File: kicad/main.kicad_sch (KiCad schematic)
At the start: 21 parts, among them J1 ICSP header, J2 LOAD+, J3 LOAD-, J4 BAT+, J5 BAT-, SW1 SW_SPST, U1 ATtiny13-20SS, U2 AO3406

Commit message: light duration settings
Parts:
- SW1: footprint Button_Switch_SMD:SW_Push_SPST_NO_Alps_SKRK -> Button_Switch_THT:SW_PUSH_6mm
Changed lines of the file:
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@@
     (property "Reference" "SW1" (id 0) (at 167.64 133.985 0))
     (property "Value" "SW_SPST" (id 1) (at 167.64 136.7601 0))
-    (property "Footprint" "Button_Switch_SMD:SW_Push_SPST_NO_Alps_SKRK" (id 2) (at 170.18 131.445 0)
+    (property "Footprint" "Button_Switch_THT:SW_PUSH_6mm" (id 2) (at 170.18 131.445 0)
       (effects (font (size 1.27 1.27)) hide)
     )
@@
     )
     (path "/02eed7f8-646e-4c7f-abe4-21cd29a1e93f"
-      (reference "SW1") (unit 1) (value "SW_SPST") (footprint "Button_Switch_SMD:SW_Push_SPST_NO_Alps_SKRK")
+      (reference "SW1") (unit 1) (value "SW_SPST") (footprint "Button_Switch_THT:SW_PUSH_6mm")
     )
     (path "/a5624d14-534e-4568-b415-af0009b2ac24"

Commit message: clean up
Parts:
- removed D1: RED, LED_SMD:LED_0805_2012Metric, symbol Device:LED
- removed H2: MountingHole, MountingHole:MountingHole_2.2mm_M2, symbol Mechanical:MountingHole
- removed J2: LOAD+, Connector_Pin:Pin_D1.0mm_L10.0mm, symbol Connector:Conn_01x01_Female
- removed J3: LOAD-, Connector_Pin:Pin_D1.0mm_L10.0mm, symbol Connector:Conn_01x01_Female
- removed R2: LDR, Connector_PinSocket_2.54mm:PinSocket_2x01_P2.54mm_Vertical, symbol Device:R_US
- removed R3: 10k, Resistor_SMD:R_0805_2012Metric, symbol Device:R_US
- added J2: Conn_LOAD, Connector_JST:JST_XH_B2B-XH-A_1x02_P2.50mm_Vertical, symbol Connector:Conn_01x02_Female
- added R2: LDR07, OptoDevice:R_LDR_5.1x4.3mm_P3.4mm_Vertical, symbol Sensor_Optical:LDR07
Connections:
- net MOSI is gone; now on net GATE: J1.4 (Pin_4), U1.5 (PB0)
- net GND: now also R2.2
- net VCC: now also J2.1 (Pin_1); no longer R1.2
- net V_REF: now also U1.3 (PB4), R2.1; no longer U1.2 (PB3)
- net at D2.1 (K), U2.3 (D): now also J2.2 (Pin_2)
- net GATE: now reaches R5.2
- net GATE: no longer U1.3 (PB4)
- new net ADC_PWR: R1.2, U1.2 (PB3)
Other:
- note added: "internal pull-up"
- moved on the sheet: D2, J1, R1, R5, R6, R7, SW1, U2

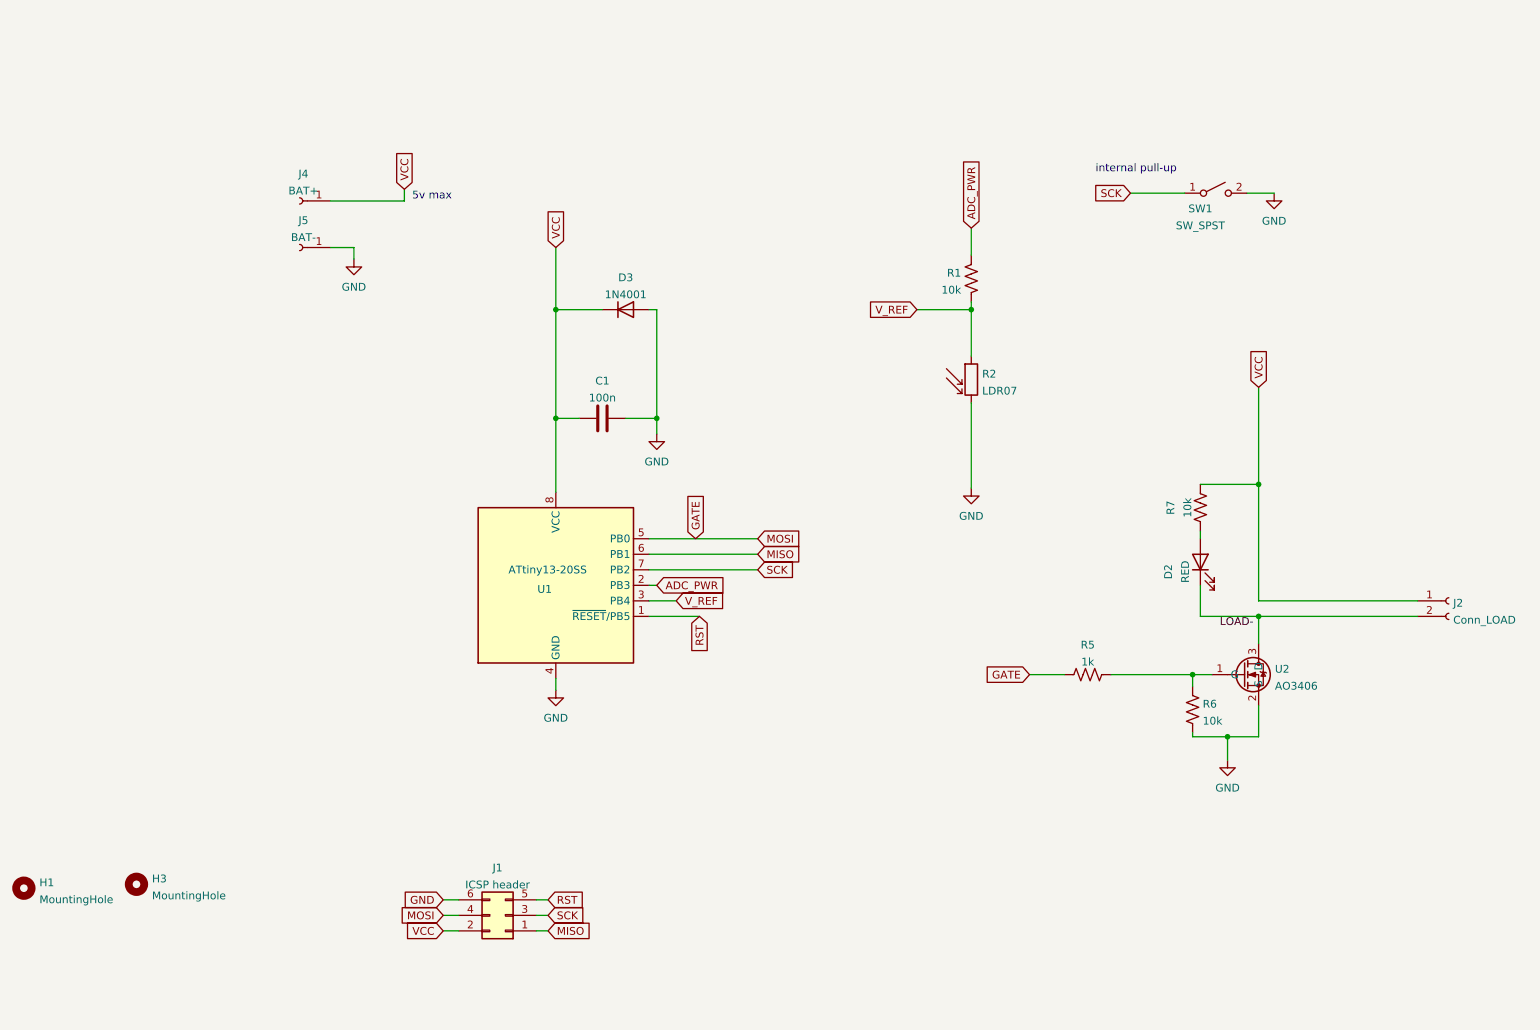
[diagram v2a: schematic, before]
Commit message: add README description and images
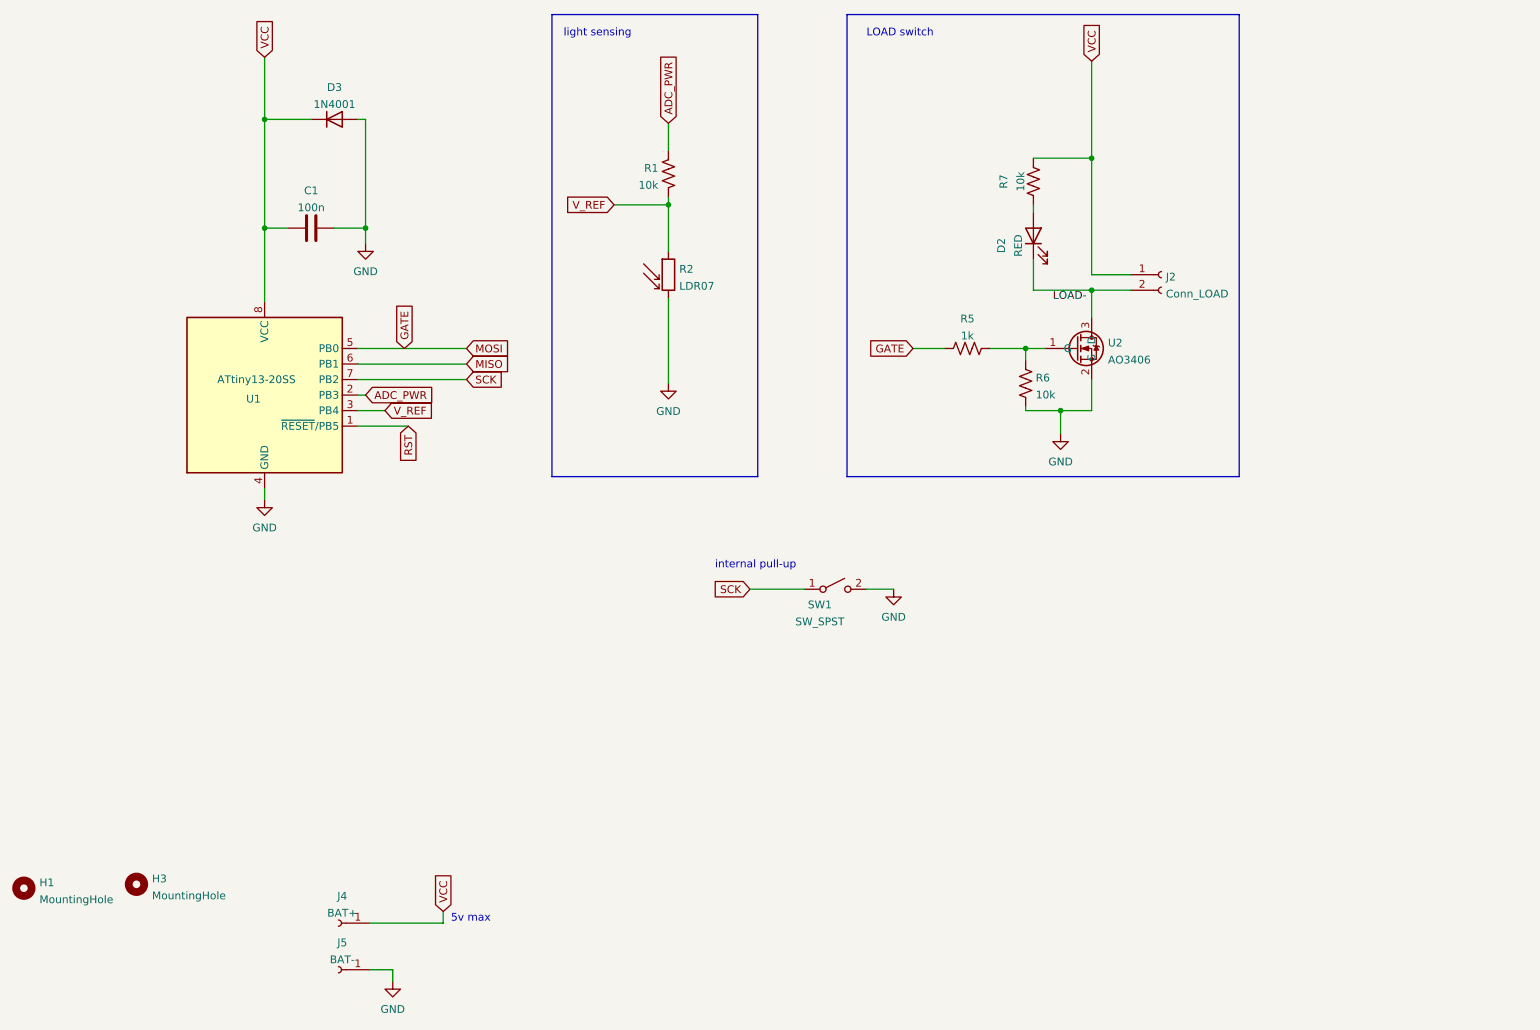
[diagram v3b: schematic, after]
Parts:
- removed J1: ICSP header, Connector_PinHeader_2.54mm:PinHeader_2x03_P2.54mm_Vertical, symbol Connector_Generic:Conn_02x03_Odd_Even
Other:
- note added: "LOAD switch"
- note added: "light sensing"
- moved on the sheet: C1, D2, D3, J2, J4, J5, R1, R2, R5, R6, R7, SW1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
